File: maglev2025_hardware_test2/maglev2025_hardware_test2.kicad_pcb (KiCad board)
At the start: 4 copper layers, 100 x 100 mm, 186 parts, among them J1 SWD, J2 PWRIn, J3 Conn_01x04, J4 Conn_01x04_MountingPin, J5 USB_C_Receptacle_USB2.0, J6 Conn_01x04, Q1 AO3400A, SW4 RotaryEncoder_Switch_MP, U1 RY8411, U10 INA240A1PW, U11 INA240A1PW, U12 INA240A1PW, U13 TPS5430DDA, U2 TMAG5170-Q1, U3 STM32G474RBTx, U4 RS3236, U5 AT8236, U6 AT8236, U7 AT8236, U8 AT8236, U9 INA240A1PW, Y1 25MHz

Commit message: finish layout, checking in progress
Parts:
- moved R34 8.53 mm to (55.3, 137.1)
- moved R35 5.79 mm to (55.3, 135.6)
- moved SW4 0.50 mm to (54.8, 121.8)
- moved C6 0.38 mm to (59.4, 144.5)
- moved Q1 0.37 mm to (53.1, 133.0), turned to 180 degrees
- moved C45 0.26 mm to (134.7, 138.0)
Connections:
- C55 pad 1: +5V -> +5V_BLINK
- J4 pad 3: +5V -> +5V_BLINK
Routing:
- net +5V_BLINK: track 6.81 -> 425.6 mm, vias 0 -> 50
- net +3.3V: track 0.00 -> 250.1 mm, vias 0 -> 140
- net GND: track 0.00 -> 150.2 mm, vias 0 -> 312
- net VREF: track 0.00 -> 96.3 mm, vias 0 -> 5
- net VPP: track 0.00 -> 30.0 mm, vias 0 -> 2
- net BUZZER: track 27.0 -> 18.7 mm
- net Net-(J5-SHIELD): track 11.4 -> 18.2 mm
- net CTRL_D1: track 44.9 -> 46.3 mm
- net Net-(R52-Pad2): track 20.0 -> 21.3 mm
- net GND_PWR: track 40.9 -> 39.8 mm
- net CTRL_D2: track 41.6 -> 42.7 mm
- net /UCPD1_CC1: track 23.3 -> 24.3 mm
- net /UCPD1_CC2: track 27.6 -> 28.2 mm
- net ISENSE_D_MCU: track 15.5 -> 14.9 mm
- net Net-(BZ1--): vias 10 -> 11
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- added copper zone on F.Cu, net +3.3V
- added copper zone on In2.Cu, net +3.3V
- added copper zone on B.Cu, net /5V
- added copper zone on B.Cu, net GND
- added copper zone on F.Cu, net GND
- added copper zone on In1.Cu, net GND
- added copper zone on In2.Cu, net GND
- added copper zone on B.Cu, net VPP
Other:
- board text added: "MAGLEV2025_V0.2 ELEC3300 Proj by RY OFR"
- board text removed: "MAGLEV2025_V0.1 ELEC3300 Proj by RY OFR"

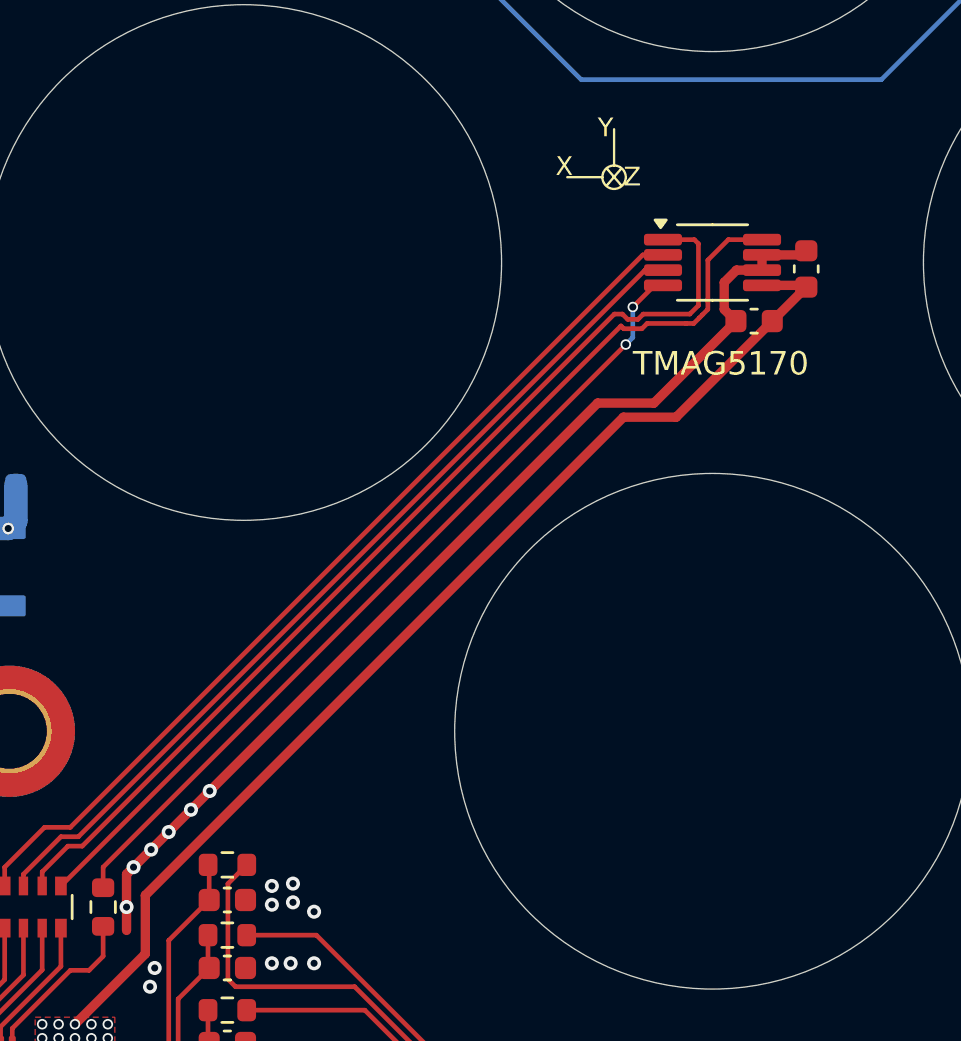
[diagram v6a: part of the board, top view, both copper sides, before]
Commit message: adding external hal connector
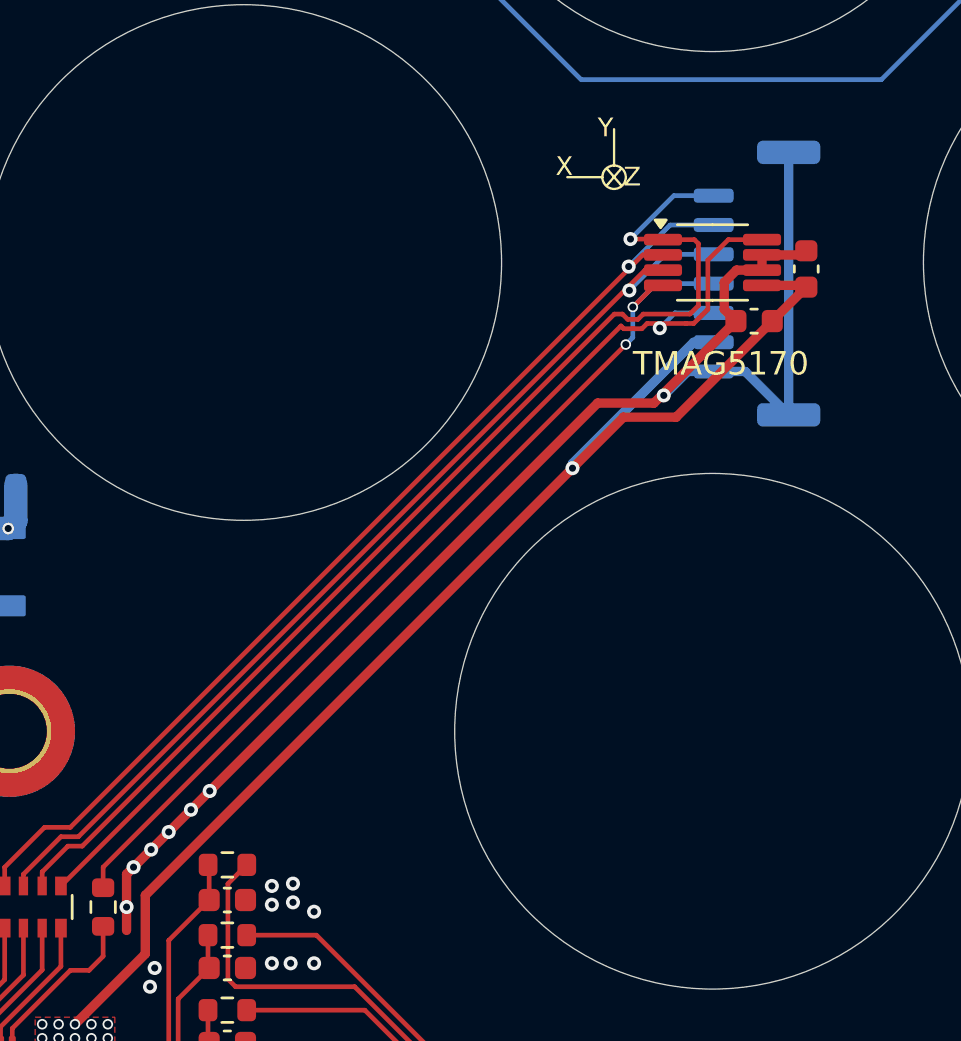
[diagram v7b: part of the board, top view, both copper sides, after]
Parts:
- added J8: Conn_01x07_MountingPin, Connector_JST:JST_GH_SM07B-GHS-TB_1x07-1MP_P1.25mm_Horizontal, B.Cu at (101.9, 100.9)
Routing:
- net GND: track 150.2 -> 167.9 mm, vias 312 -> 313
- net +3.3V: track 250.1 -> 258.5 mm, vias 140 -> 141
- net SPI1_SCK: track 43.0 -> 48.7 mm, vias 0 -> 1
- net SPI1_MOSI: track 39.8 -> 44.2 mm, vias 0 -> 1
- net SPI1_MISO: track 38.5 -> 42.7 mm, vias 0 -> 1
- net ~{MAG_CS}: track 35.8 -> 39.7 mm
- net ~{MAG_ALRT}: track 42.7 -> 45.2 mm, vias 0 -> 1
